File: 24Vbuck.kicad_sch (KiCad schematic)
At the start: 0 parts

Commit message: pm
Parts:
- added C1, C_C1, C_C2, C_C3: C, symbol Device:C
- added R_C1, R_UV1, R_UV2: R, LM5146RGYR:IC_LM5146RGYR, symbol Device:R
- added R_C2, R_FB1, R_FB2: R, symbol Device:R
- added R_RT: 24.9, LM5146RGYR:IC_LM5146RGYR, symbol Device:R
- added U2: LM5146RGYR, LM5146RGYR:IC_LM5146RGYR, symbol LM5146RGYR:LM5146RGYR
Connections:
- new net: C1.2, R_RT.2, U2.2 (RT)
- new net: C_C2.2, R_C1.2, R_FB1.2, R_FB2.1, U2.5 (FB)
- new net: R_UV1.2, R_UV2.2, U2.1 (EN/UVLO)
- new net: C_C1.1, C_C2.1, U2.4 (COMP)
- new net: C_C3.1, R_C2.2
- new net: C_C1.2, R_C1.1
- new net: U2.16 (NC), U2.9 (NC)
- new net 24VPGOOD: U2.10 (PGOOD)
- new net 24Vsync_inn: U2.8 (SYNCIN)
- new net 24Vsync_out: U2.7 (SYNCOUT)
- new net EP: U2.15 (EP), U2.21 (EP)
- new net GND: C1.1, R_FB2.2, R_RT.1, R_UV2.1, U2.6 (AGND)
- new net Vout: R_C2.1, R_FB1.1

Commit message: LM5146 etter skjema
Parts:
- added C_BST, C_ILIM, C_IN, C_OUT, C_VCC: C, symbol Device:C
- added C_RC, C_deco: 0.1u, symbol Device:C
- added L1: L, symbol Device:L
- added Q3, Q4: NMOS, NVMFD5C674NLT1G, symbol Simulation_SPICE:NMOS
- added R_LIM, R_PG: R, symbol Device:R
- added R_RC: 4.7, symbol Device:R
- renumbered C1 to C_SS
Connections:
- net 24VPGOOD: now also R_PG.1
- net GND: now also C_ILIM.2, C_RC.2, C_VCC.2; no longer U2.6 (AGND)
- net at R_RT.2, U2.2 (RT): no longer C_SS.2
- net FB: now reaches C_C2.2, R_C1.2, R_FB1.2, R_FB2.1, U2.5 (FB)
- net COMP: now reaches C_C1.1, C_C2.1, U2.4 (COMP)
- net at R_UV1.1: now also U2.14 (VCC), U2.20 (VIN), U2.6 (AGND), C_IN.1, C_VCC.1, Q3.1 (D), R_PG.2, R_RC.1
- net at U2.11 (ILIM): now also C_ILIM.1, R_LIM.1
- net PGND: now reaches U2.12 (PGND)
- net PGND: now also C_IN.2, C_OUT.2, Q4.3 (S)
- net at U2.13 (LO): now also Q4.2 (G)
- net at U2.17 (BST): now also C_BST.1
- net at U2.18 (HO): now also Q3.2 (G)
- net at U2.19 (SW): now also C_BST.2, L1.1, Q3.3 (S), Q4.1 (D), R_LIM.2
- net at U2.3 (SS/TRK): now also C_SS.2
- new net 24V_VINN: C_RC.1, R_RC.2
- new net 24V_VOUT: C_OUT.1, L1.2
- no-connect marks 0 -> 2
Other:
- note added: "An RC filter from the input rail to the VIN pin (for example, 4.7 Ω and 0.1 µF) provides supplementary filtering at the VIN pin."
- moved on the sheet: C_C1, C_C2, C_C3, R_C1, R_C2, R_FB1, R_FB2, R_UV1, R_UV2

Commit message: Sette opp simuering
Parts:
- removed C_deco: 0.1u, symbol Device:C
- added C_IN2, C_IN3: 4.7uF, symbol Device:C
- added C_OUT2, C_OUT3: 10uF, symbol Device:C
- added Q5: NVMFD010N10MCLT1G, Marinor:NVMFD5C674NLT1G, symbol Aase:NVMFD010N10MCLT1G
- added R1: 1, symbol Device:R
- added R2: 1m, symbol Device:R
- added R_Load1: 4.8, symbol Device:R
- added V1: 48, Package_SON:WSON-8-1EP_6x5mm_P1.27mm_EP3.4x4mm, symbol Simulation_SPICE:VDC
- 68nF1: renamed from C_SS; value C -> C_SS
- C_BST2: renamed from C_BST; value C -> 0.1uF
- C_C1: value C -> 3.9nF
- C_C2: value C -> 120pF
- C_C3: value C -> 1000pF
- C_ILIM1: renamed from C_ILIM; value C -> 12pF
- C_IN1: renamed from C_IN; value C -> 4.7uF
- C_OUT1: renamed from C_OUT; value C -> 10uF
- C_VCC1: renamed from C_VCC; value C -> 2.2uF
- L_o1: renamed from L1; value L -> 15uH
- R_C1: value R -> 6.65k
- R_C2: value R -> 23.7
- R_FB1: value R -> 20.4k
- R_FB2: value R -> 0.698k
- R_LIM1: renamed from R_LIM; value R -> 442
- R_PG1: renamed from R_PG; value R -> 20k
- R_RT2: renamed from R_RT; value 24.9 -> 24.9k
- R_UV1: value R -> 301k
- R_UV2: value R -> 11.3k
- renumbered C_RC to C_RC1, R_RC to R_RC1
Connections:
- net Vout is gone; now on net 24V_VOUT: R_C2.1, R_FB1.1
- net 24V_VINN: now also C_IN1.1, Q3.1 (D), R_UV1.1, V1.1; no longer C_RC1.1
- net 24V_VOUT: now also R_Load1.1
- net 24Vsync_inn: now also R1.2
- net FB: now also C_C3.2
- net PGND: now also C_IN3.2, C_OUT3.2, R2.2; no longer C_IN1.2, C_OUT1.2
- net at U2.3 (SS/TRK): now also 68nF1.1; no longer 68nF1.2
- net GND renamed 0
- net 0: now also 68nF1.2, U2.6 (AGND), R1.1, R2.1, R_Load1.2, V1.2; no longer 68nF1.1
- new net: C_VCC1.1, R_PG1.2, U2.14 (VCC)
- new net: C_RC1.1, R_RC1.1, U2.20 (VIN)
- new net: C_IN1.2, C_IN2.1
- new net: C_IN2.2, C_IN3.1
- new net: C_OUT1.2, C_OUT2.1
- new net: C_OUT2.2, C_OUT3.1
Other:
- note added: "C_in = 10uF"
- note added: "R_UV2 og U_UV1 Disse to ser hele bussen eller SW-noden, spenningen kan stige mot 85-100 V under en transient."
- note added: "c_out = 25uF"
- moved on the sheet: 68nF1, C_C1, C_C2, C_C3, C_IN1, C_OUT1, C_RC1, L_o1, R_C1, R_C2, R_FB1, R_FB2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

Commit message: valgte verdier, ikke modellnr
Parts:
- removed 68nF1: C_SS, symbol Device:C
- removed Q3, Q4: NMOS, NVMFD5C674NLT1G, symbol Simulation_SPICE:NMOS
- removed R_FB1: 20.4k, symbol Device:R
- removed R_FB2: 0.698k, symbol Device:R
- added C_SS2: 68nF, symbol Device:C
- added R_FB3: 20.4k, symbol Device:R
- added R_FB4: 0.698k, symbol Device:R
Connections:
- net PGND is gone; now on net EP: C_IN3.2, C_OUT3.2, R2.2, U2.12 (PGND)
- net 0: now also C_SS2.2, R_FB4.2
- net 24V_VINN: now also C_IN2.1, C_IN3.1, Q5.10 (D1_3), Q5.12 (D1_4), Q5.14 (D1_5), Q5.16 (D1_6), Q5.7 (D1_1), Q5.8 (D1_2)
- net 24V_VOUT: now also C_OUT2.1, C_OUT3.1, R_FB3.1
- net EP: now also C_IN1.2, C_IN2.2, C_OUT1.2, C_OUT2.2, Q5.3 (S2)
- net FB: now also R_FB3.2, R_FB4.1
- net at U2.3 (SS/TRK): now also C_SS2.1
- net at C_BST2.2, L_o1.1, R_LIM1.2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: now also Q5.1 (S1), Q5.11 (D2_4), Q5.13 (D2_5), Q5.15 (D2_6), Q5.5 (D2_1), Q5.6 (D2_2), Q5.9 (D2_3)
- net at Q5.2 (G1): now also U2.18 (HO)
- net at Q5.4 (G2): now also U2.13 (LO)
- no-connect marks 2 -> 1
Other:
- moved on the sheet: Q5

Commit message: Fysiske komp for 24V
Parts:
- removed C_BST2: 0.1uF, symbol Device:C
- removed C_C1: 3.9nF, symbol Device:C
- removed C_C2: 120pF, symbol Device:C
- removed C_C3: 1000pF, symbol Device:C
- removed C_ILIM1: 12pF, symbol Device:C
- removed C_IN1, C_IN2, C_IN3: 4.7uF, symbol Device:C
- removed C_OUT1, C_OUT2, C_OUT3: 10uF, symbol Device:C
- removed C_RC1: 0.1u, symbol Device:C
- removed C_SS2: 68nF, symbol Device:C
- removed C_VCC1: 2.2uF, symbol Device:C
- removed L_o1: 15uH, symbol Device:L
- removed R1: 1, symbol Device:R
- removed R2: 1m, symbol Device:R
- removed R_C1: 6.65k, LM5146RGYR:IC_LM5146RGYR, symbol Device:R
- removed R_C2: 23.7, symbol Device:R
- removed R_FB3: 20.4k, symbol Device:R
- removed R_FB4: 0.698k, symbol Device:R
- removed R_LIM1: 442, symbol Device:R
- removed R_Load1: 4.8, symbol Device:R
- removed R_PG1: 20k, symbol Device:R
- removed R_RC1: 4.7, symbol Device:R
- removed R_RT2: 24.9k, LM5146RGYR:IC_LM5146RGYR, symbol Device:R
- removed R_UV2: 11.3k, LM5146RGYR:IC_LM5146RGYR, symbol Device:R
- removed V1: 48, Package_SON:WSON-8-1EP_6x5mm_P1.27mm_EP3.4x4mm, symbol Simulation_SPICE:VDC
- added C1: 120pF, CGA3E2C0G1H121J080AA:CAPC1608X90N, symbol Aase:CGA3E2C0G1H121J080AA
- added C200?: 2.2uF, CGA4J3X7R1E225K125AB:CAPC2012X145N, symbol Aase:CGA4J3X7R1E225K125AB
- added C200? (x2): 0.1uF, CGA4J2X7R2A104K125AA:CAPC2012X145N, symbol Aase:CGA4J2X7R2A104K125AA
- added C200?: 3.9nF, CGA3E1C0G2A392J080AC:CAPC1608X90N, symbol Aase:CGA3E1C0G2A392J080AC
- added C200?: 68nF, CGA3E2X7R1H683K080AA:CAPC1608X90N, symbol Aase:CGA3E2X7R1H683K080AA
- added C200?: 12pF, CGA3E2C0G2A120J080AA:CAPC1608X90N, symbol Aase:CGA3E2C0G2A120J080AA
- added C200?: 1000pF, CGA3E2C0G1H102J080AA:CAPC1608X90N, symbol Aase:CGA3E2C0G1H102J080AA
- added C201, C202, C203, C20? (x5): 2.2uF, Capacitor_SMD:C_0603_1608Metric_Pad1.08x0.95mm_HandSolder, symbol Device:C
- added C20?: 10uF, Capacitor_SMD:C_1210_3225Metric_Pad1.33x2.70mm_HandSolder, symbol Device:C
- added L2001: 15uH, WE-XHMI_1510:WE-XHMI_1510, symbol Aase:WE-XHMI_1510
- added R20?: 20k, Resistor_SMD:R_0603_1608Metric_Pad0.98x0.95mm_HandSolder, symbol Device:R
- added R20?: 23.7, Resistor_SMD:R_0603_1608Metric_Pad0.98x0.95mm_HandSolder, symbol Device:R
- added R20?: 0, Resistor_SMD:R_0603_1608Metric_Pad0.98x0.95mm_HandSolder, symbol Device:R
- added R20?: 11.3k, Resistor_SMD:R_0603_1608Metric_Pad0.98x0.95mm_HandSolder, symbol Device:R
- added R20?: 6.65k, Resistor_SMD:R_0603_1608Metric_Pad0.98x0.95mm_HandSolder, symbol Device:R
- added R20?: 20.4k, Resistor_SMD:R_0603_1608Metric_Pad0.98x0.95mm_HandSolder, symbol Device:R
- added R20?: 4.7, Resistor_SMD:R_0603_1608Metric_Pad0.98x0.95mm_HandSolder, symbol Device:R
- added R20?: 0.698k, Resistor_SMD:R_0603_1608Metric_Pad0.98x0.95mm_HandSolder, symbol Device:R
- added R20?: 442, Resistor_SMD:R_0805_2012Metric_Pad1.20x1.40mm_HandSolder, symbol Device:R
- added R20?: 24.9k, Resistor_SMD:R_0603_1608Metric_Pad0.98x0.95mm_HandSolder, symbol Device:R
- R20?: renamed from R_UV1; footprint LM5146RGYR:IC_LM5146RGYR -> Resistor_SMD:R_0805_2012Metric; DatasheetValue (none) -> R_UV1; MF (none) -> Panasonic; MP (none) -> ERJ-6ENF3013V
- renumbered Q5 to Q?, U2 to U?
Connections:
- net 24VPGOOD: now also R20?.2
- net 24V_VINN: now also C20?.1, C20?.1, C20?.1, C20?.1, C20?.1, C20?.1, R20?.1
- net 24V_VOUT: now also C201.1, C202.1, C203.1, L2001.2, R20?.2, R20?.2
- net COMP: now also C1.2, C200?.2
- net EP: now also C201.2, C202.2, C203.2, C20?.2, C20?.2, C20?.2, C20?.2, C20?.2, C20?.2
- net FB: now also C1.1, C200?.1, R20?.1, R20?.2, R20?.2
- net at U?.20 (VIN): now also C200?.2, R20?.2
- net at R20?.2, U?.1 (EN/UVLO): now also R20?.1
- net at U?.11 (ILIM): now also C200?.2, R20?.2
- net at U?.14 (VCC): now also C200?.2, R20?.1
- net at U?.17 (BST): now also R20?.2
- net at Q?.1 (S1), Q?.11 (D2_4), Q?.13 (D2_5)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: now also C200?.1, L2001.1, R20?.1
- net at U?.2 (RT): now also R20?.1
- net at U?.3 (SS/TRK): now also C200?.2
- net 0 renamed GND
- net GND: now also C200?.1, C200?.1, C200?.1, C200?.1, R20?.1, R20?.2, R20?.2
- new net: C200?.2, R20?.1 (x2)
- new net: C200?.1, R20?.1

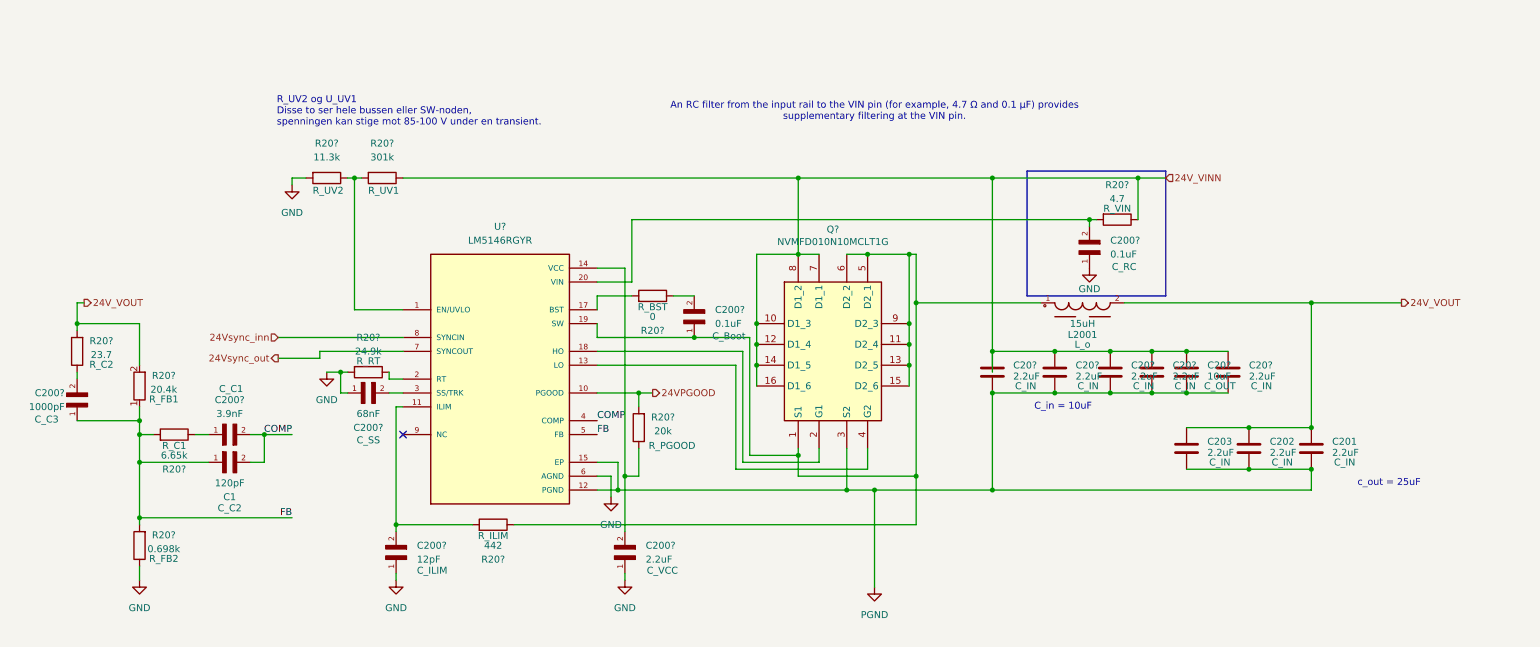
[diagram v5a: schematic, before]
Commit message: Bytta kondensatorer til Wurth
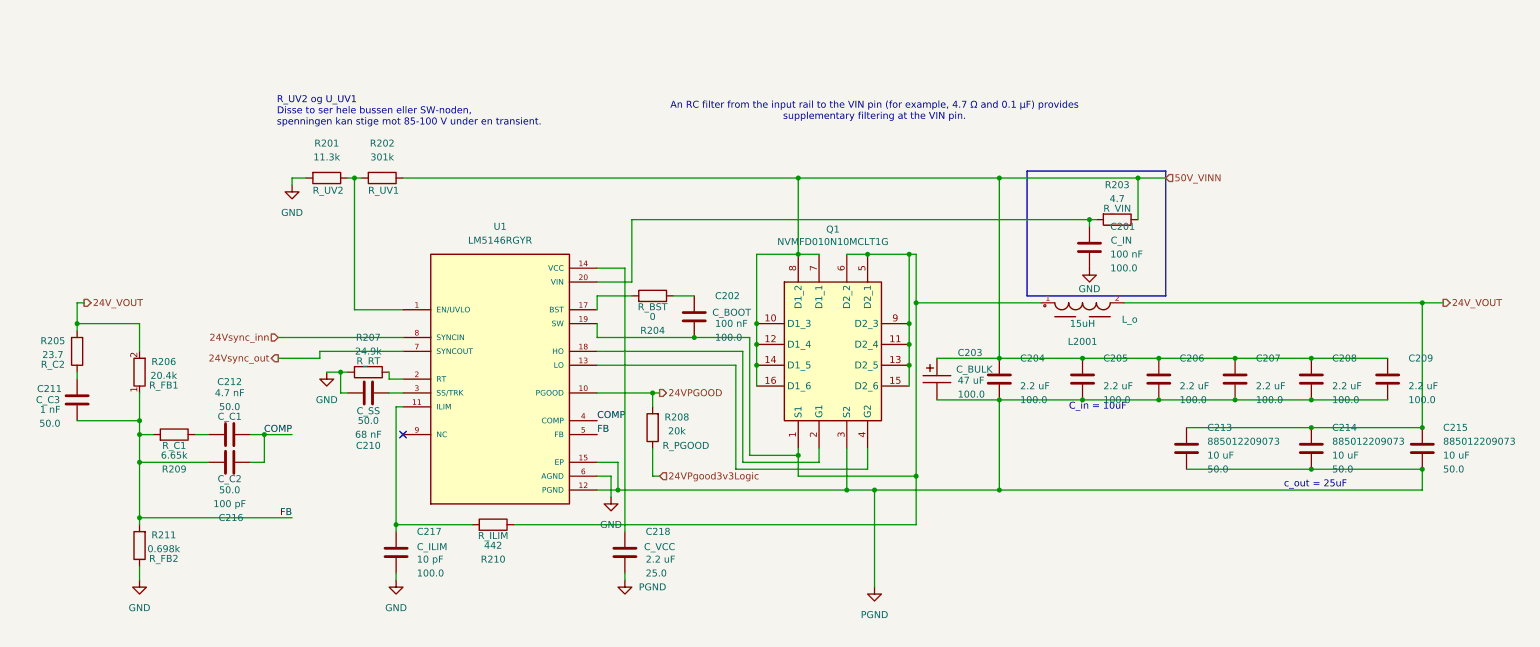
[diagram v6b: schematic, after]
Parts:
- removed C1: 120pF, CGA3E2C0G1H121J080AA:CAPC1608X90N, symbol Aase:CGA3E2C0G1H121J080AA
- removed C200?: 2.2uF, CGA4J3X7R1E225K125AB:CAPC2012X145N, symbol Aase:CGA4J3X7R1E225K125AB
- removed C200? (x2): 0.1uF, CGA4J2X7R2A104K125AA:CAPC2012X145N, symbol Aase:CGA4J2X7R2A104K125AA
- removed C200?: 3.9nF, CGA3E1C0G2A392J080AC:CAPC1608X90N, symbol Aase:CGA3E1C0G2A392J080AC
- removed C200?: 68nF, CGA3E2X7R1H683K080AA:CAPC1608X90N, symbol Aase:CGA3E2X7R1H683K080AA
- removed C200?: 12pF, CGA3E2C0G2A120J080AA:CAPC1608X90N, symbol Aase:CGA3E2C0G2A120J080AA
- removed C200?: 1000pF, CGA3E2C0G1H102J080AA:CAPC1608X90N, symbol Aase:CGA3E2C0G1H102J080AA
- removed C201, C202, C203, C20? (x5): 2.2uF, Capacitor_SMD:C_0603_1608Metric_Pad1.08x0.95mm_HandSolder, symbol Device:C
- removed C20?: 10uF, Capacitor_SMD:C_1210_3225Metric_Pad1.33x2.70mm_HandSolder, symbol Device:C
- added C201, C202: 100 nF, Capacitor_SMD_Wurth:C_Wurth_WCAP-CSGP-0603_R, symbol Aase:0603_R_885012206120
- added C203: 47 uF, Capacitor_SMD_Wurth:CP_Wurth_WCAP-ASLI-D12.5L14, symbol Aase:D12.5L14_865080862008
- added C204, C205, C206, C207, C208, C209: 2.2 uF, Capacitor_SMD_Wurth:C_Wurth_WCAP-CSGP-1210_H2.5, symbol Aase:1210_H2.5_885012209071
- added C210: 68 nF, Capacitor_SMD_Wurth:C_Wurth_WCAP-CSGP-0603_R, symbol Aase:0603_R_885012206094
- added C211: 1 nF, Capacitor_SMD_Wurth:C_Wurth_WCAP-CSGP-0603_R, symbol Aase:0603_R_885012006063
- added C212: 4.7 nF, Capacitor_SMD_Wurth:C_Wurth_WCAP-CSGP-0805_H1.25_R, symbol Aase:0805_H1.25_R_885012007067
- added C213, C214, C215: 10 uF, Capacitor_SMD_Wurth:C_Wurth_WCAP-CSGP-1210_H2.5, symbol Aase:1210_H2.5_885012209073
- added C216: 100 pF, Capacitor_SMD_Wurth:C_Wurth_WCAP-CSGP-0603_R, symbol Aase:0603_R_885012006057
- added C217: 10 pF, Capacitor_SMD_Wurth:C_Wurth_WCAP-CSGP-0603_R, symbol Aase:0603_R_885012006073
- added C218: 2.2 uF, Capacitor_SMD_Wurth:C_Wurth_WCAP-CSGP-0805_H1.25_R, symbol Aase:0805_H1.25_R_885012207079
- gave numbers to parts that had none: 13
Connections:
- net 24V_VOUT: now also C213.1, C214.1, C215.1
- net COMP: now also C212.2, C216.1
- net EP: now also C203.2, C204.2, C205.2, C206.2, C207.2, C208.2, C209.2, C213.2, C214.2, C215.2, C218.2
- net FB: now also C211.2, C216.2
- net GND: now also C201.2, C210.1, C217.2
- net at R210.2, U1.11 (ILIM): now also C217.1
- net at U1.14 (VCC): now also C218.1; no longer R208.1
- net at L2001.1, Q1.1 (S1), Q1.11 (D2_4)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: now also C202.2
- net at R203.2, U1.20 (VIN): now also C201.1
- net at U1.3 (SS/TRK): now also C210.2
- net at R205.1: now also C211.1
- net at R209.1: now also C212.1
- net at R204.1: now also C202.1
- net 24V_VINN renamed 50V_VINN
- net 50V_VINN: now also C203.1, C204.1, C205.1, C206.1, C207.1, C208.1, C209.1
- new net 24VPgood3v3Logic: R208.1
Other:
- moved on the sheet: R205, R206, R208
